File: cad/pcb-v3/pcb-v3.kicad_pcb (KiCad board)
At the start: 4 copper layers, 19.3 x 19.3 mm, 50 parts

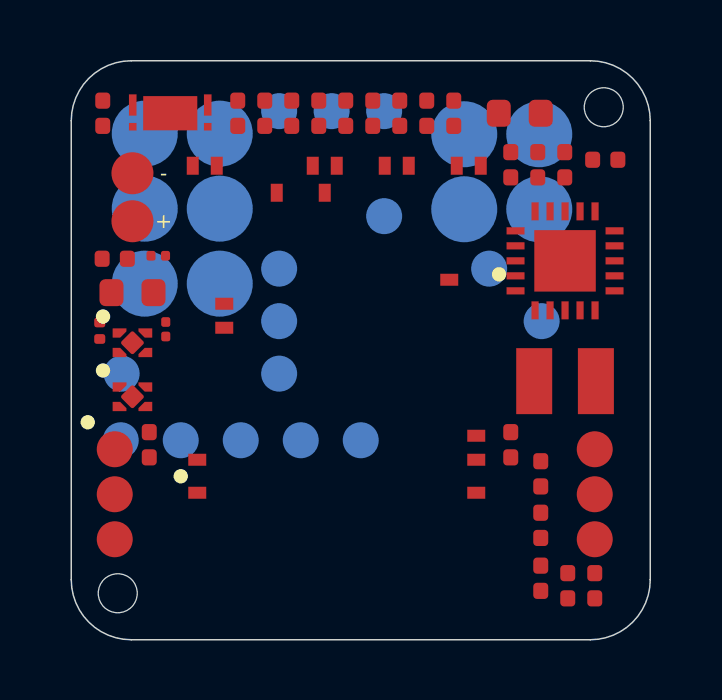
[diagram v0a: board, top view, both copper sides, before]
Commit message: Routing: 3 opens left, and none of them are the PCM's
Placing the 0201s nearest-to-U5 was the wrong objective and it was mine. It
walked R8/R9/C14 up the LEFT STRIP -- 2.72 mm wide, already carrying U3, U4
(X2SON-4, pads 0.34-0.40 apart) and C5 -- and the opens came back clustered on
exactly those parts. They are now scored by ELBOW ROOM within a bounded radius
of U5 instead.

  before: 10-12 open pads pre-stitch, 4 NO PATH after
  after :  4 open pads pre-stitch, 3 NO PATH after

PCM_VDD R8.2 and BL_RETURN R6.1 are gone -- the parts the PCM added now route.

Bounded, not free: pure elbow room threw R9 21.5 mm into the far corner, and
R9 is the V- sense leg, a high-impedance node feeding a comparator that trips
on 20 mV. Distance there is an aerial, not a resistance. SMALL_NEAR caps the
trade. Removing the cluster gate on U5 also mattered: it had dragged U5 itself
from 2.28 to 8.81 mm off the cell pad chasing a target the new objective does
not optimise.

Remaining 3 (VBAT U2.18, VBAT_OK U2.13, VSTOR U4.4) are the U2/U4 knot
ROUTING-RESULT.md named as this board's hard corner before the PCM existed --
0.5 mm-pitch QFN, 0.26 mm pad gaps, ~0.21 mm of escape ring per side. They
resist the router in six configurations and handroute at correct rules.

Also: router and gnd_taps now use 0.45/0.20 vias, JLC's documented standard
floor (preflight check 8) rather than the conservative 0.6/0.3. Taps went
16 -> 21 on the earlier board.
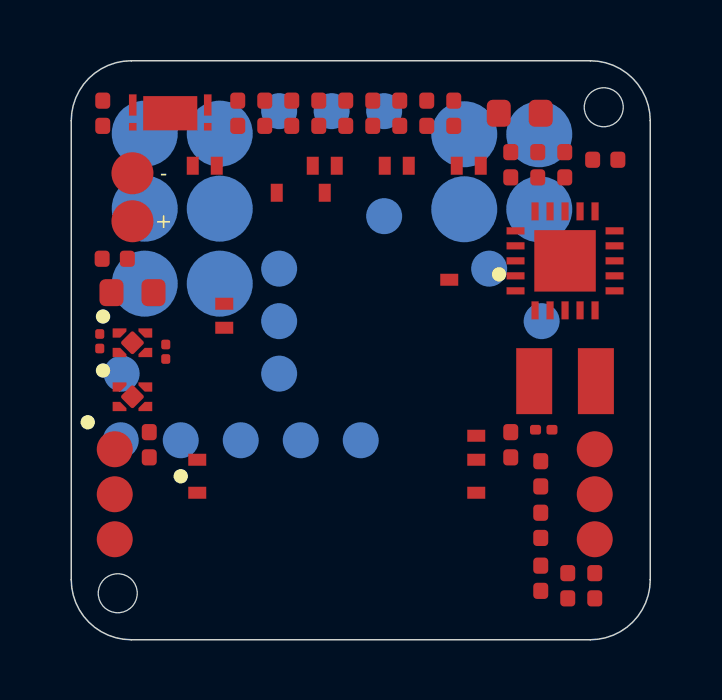
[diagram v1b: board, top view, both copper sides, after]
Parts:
- moved C14 15.2 mm to (6.10, 2.65), turned to 0 degrees
- moved R8 3.21 mm to (-6.50, 0.05), turned to 90 degrees
- moved R9 2.24 mm to (-8.70, -0.30)
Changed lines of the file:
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@@
 	(footprint "touchid:R8"
 		(layer "F.Cu")
-		(at -6.75 -3.15)
+		(at -6.5 0.05 90)
 		(property "Reference" "R8"
 			(at 0 0 0)
@@
 	(footprint "touchid:R9"
 		(layer "F.Cu")
-		(at -6.5 -0.7 90)
+		(at -8.7 -0.3 90)
 		(property "Reference" "R9"
 			(at 0 0 0)
@@
 	(footprint "touchid:C14"
 		(layer "F.Cu")
-		(at -8.7 -0.65 90)
+		(at 6.1 2.65)
 		(property "Reference" "C14"
 			(at 0 0 0)

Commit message: Fine-pitch escape ring: U3/U4 get a reserved 0.55 mm ring; 3 blockers
Five of the ten open pads were on U3/U4, and the cause was structural: they are
TPS7A2033 in X2SON-4 with pads 0.34-0.40 mm apart, so nothing routes BETWEEN
their pins at 0.127/0.10 -- every pin must escape radially. R8 sat 1.11 mm to
one side, R9 1.09 mm to the other, TP6 directly above, C5 below. U4 was boxed
in on four sides.

The packer could not know. Worse, the elbow-room objective I added earlier
actively PREFERRED those spots, because the gap beside a fine-pitch part is the
emptiest-looking space on the board. FINE_PITCH/FINE_ESCAPE now reserves a
0.55 mm ring in _legal_mask, at the source, and the 0201 objective goes back to
nearest-U5 since it no longer has to carry a job that was never its own.

  open pads 10 -> 9, and stage 1 routes 9/9 with the pogo keep-outs in place

TWO SELF-INFLICTED BUGS FOUND AND FIXED ALONG THE WAY:

* The 0201 scoring ranked by distance WITHIN a rotation and by free space
  BETWEEN rotations. Two comparisons deciding the same thing, disagreeing --
  so the fix appeared to do nothing at all and R8 stayed 21.5 mm from U5.

* check_board.py flagged copper sitting EXACTLY on the 0.10 rule: shapely
  returns 0.09999999998 and  calls that a violation, printed as
  '0.1000'. The router's own check_drc passes the same board clean. Now
  compares against MIN_CU - 1e-6; a nanometre is below any fab resolution and
  well above float noise.

Also recorded a dead end: a hand-written dangling-segment remover deleted 334
of 593 segments because its 'is this end anchored' test knew about segments and
vias but FORGOT PADS. Tracks end on pads. Reverted; the board here is the
un-stitched route, which has 9 open pads but no stubs.
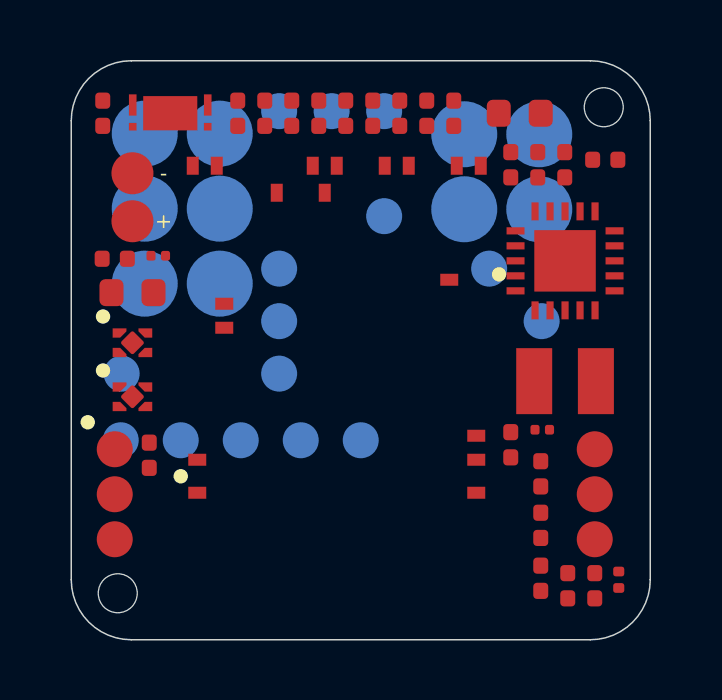
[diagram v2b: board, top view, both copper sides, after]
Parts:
- moved R9 15.0 mm to (6.05, 2.65), turned to 0 degrees
- moved C14 5.59 mm to (8.60, 7.65), turned to 90 degrees
- moved R8 3.21 mm to (-6.75, -3.15), turned to 0 degrees
- moved C8 0.35 mm to (-7.05, 3.50)
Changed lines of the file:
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@@
 	(footprint "touchid:R8"
 		(layer "F.Cu")
-		(at -6.5 0.05 90)
+		(at -6.75 -3.15)
 		(property "Reference" "R8"
 			(at 0 0 0)
@@
 	(footprint "touchid:R9"
 		(layer "F.Cu")
-		(at -8.7 -0.3 90)
+		(at 6.05 2.65)
 		(property "Reference" "R9"
 			(at 0 0 0)
@@
 	(footprint "touchid:C14"
 		(layer "F.Cu")
-		(at 6.1 2.65)
+		(at 8.6 7.65 90)
 		(property "Reference" "C14"
 			(at 0 0 0)
@@
 	(footprint "touchid:C8"
 		(layer "F.Cu")
-		(at -7.05 3.15 90)
+		(at -7.05 3.5 90)
 		(property "Reference" "C8"
 			(at 0 0 0)

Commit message: GND pads may not be ASSIGNED into a pogo no-via ring (hard ban in the packer)
The 0402/0201 assignment already had a soft _POGO_PENALTY of 40.0, reasoned
about the PART: a passive over a pogo pad has no via for its own escape and
sits where the pins flex. For a part carrying a GND pad the consequence is
harder than a penalty -- the plane is on In2.Cu, a GND pad on F.Cu reaches it
only through a via, and inside a ring no via may exist. Now a hard 1e6 cost:
104 (part, slot) pairs forbidden, and C12 moved out of J4.5's ring.

MY FIRST VERSION OF THE GLOBAL GATE WAS WRONG and I am recording why. It raised
SystemExit on any GND pad inside a ring and failed the build on EIGHT of them --
three on U1, two on U2, plus C7 and U5.4 -- all fixed-position parts that cannot
move, and most of them connected perfectly well today.

The rule I wrote was 'a GND pad may not sit in a pogo ring'. The true rule is
weaker: a GND pad needs A PATH TO GND COPPER THAT REACHES THE PLANE. Its own
via is the easy route and a ring closes it, but a track to neighbouring GND
copper does just as well -- which is exactly how U1.15, U1.32 and U2.5 are
connected right now. Being in a ring is a RISK, not a fault. Softened to a
warning that names the at-risk pads so check 6 can be read against it.

C5.2 REMAINS, and it is not a packer problem: C5 is a 0603 positioned by the
hand-written stack(), and the arithmetic says the strip cannot avoid the ring --
U3 (1.30) + U4 (1.30) + C5 (1.04) + two 0.50 gaps = 4.64 mm from y=+2.20 ends
at -2.44, while GND pads must stay above -0.795. It overruns by 1.65 mm. Three
parts do not fit above the J4 block. C5 has to leave the left strip, and where
it goes is a real design decision on a board with no spare area.
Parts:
- moved C3 15.6 mm to (6.00, 5.84)
- moved R2 12.4 mm to (3.10, -7.90)
- moved R7 8.10 mm to (-8.60, -7.90)
- moved C12 7.64 mm to (-2.30, -7.90), turned to 90 degrees
- moved R4 7.64 mm to (-8.20, -3.05), turned to 0 degrees
- moved R5 7.20 mm to (-1.40, -7.90)
- moved R6 4.50 mm to (-4.10, -7.90)
- moved ROV1 3.15 mm to (8.15, -6.35), turned to 0 degrees
- moved C6 2.70 mm to (-0.50, -7.90)
- moved C4 1.80 mm to (1.30, -7.90)
- moved C1 1.72 mm to (6.00, 4.12)
- moved ROK2 1.36 mm to (6.80, -6.18), turned to 90 degrees
- moved C10 0.93 mm to (6.90, 7.85)
- moved C2 0.93 mm to (6.00, 7.60)
- moved ROV2 0.90 mm to (5.00, -6.18)
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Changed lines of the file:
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@@
 	(footprint "touchid:C1"
 		(layer "F.Cu")
+		(at 6.0 4.119 90)
+		(property "Reference" "C1"
+			(at 0 0 0)
+			(layer "F.SilkS")
+			(hide yes)
+			(effects (font (size 0.6 0.6) (thickness 0.1)))
+		)
+		(attr smd)
+		(fp_text user "C1"
+			(at 0 0 0)
+			(layer "F.Fab")
+			(effects (font (size 0.4 0.4) (thickness 0.06)))
+		)
+		(pad "1" smd roundrect
+			(at -0.42 0)
+			(size 0.5 0.54)
+			(layers "F.Cu" "F.Mask" "F.Paste")
+			(roundrect_rratio 0.25)
+			(net 27 "VIN_DC")
+		)
+		(pad "2" smd roundrect
+			(at 0.42 0)
+			(size 0.5 0.54)
+			(layers "F.Cu" "F.Mask" "F.Paste")
+			(roundrect_rratio 0.25)
+			(net 4 "GND")
+		)
+		(model "${KIPRJMOD}/3dmodels/chip_0402.step"
+			(offset (xyz 0 0 0))
+			(scale (xyz 1 1 1))
+			(rotate (xyz 0 0 0))
+		)
+	)
+	(footprint "touchid:C2"
+		(layer "F.Cu")
+		(at 6.0 7.6 90)
+		(property "Reference" "C2"
+			(at 0 0 0)
+			(layer "F.SilkS")
+			(hide yes)
+			(effects (font (size 0.6 0.6) (thickness 0.1)))
+		)
+		(attr smd)
+		(fp_text user "C2"
+			(at 0 0 0)
+			(layer "F.Fab")
+			(effects (font (size 0.4 0.4) (thickness 0.06)))
+		)
+		(pad "1" smd roundrect
+			(at -0.42 0)
+			(size 0.5 0.54)
+			(layers "F.Cu" "F.Mask" "F.Paste")
+			(roundrect_rratio 0.25)
+			(net 30 "VSTOR")
+		)
+		(pad "2" smd roundrect
+			(at 0.42 0)
+			(size 0.5 0.54)
+			(layers "F.Cu" "F.Mask" "F.Paste")
+			(roundrect_rratio 0.25)
+			(net 4 "GND")
+		)
+		(model "${KIPRJMOD}/3dmodels/chip_0402.step"
+			(offset (xyz 0 0 0))
+			(scale (xyz 1 1 1))
+			(rotate (xyz 0 0 0))
+		)
+	)
+	(footprint "touchid:C3"
+		(layer "F.Cu")
 		(at 6.0 5.836 90)
-		(property "Reference" "C1"
-			(at 0 0 0)
-			(layer "F.SilkS")
-			(hide yes)
-			(effects (font (size 0.6 0.6) (thickness 0.1)))
-		)
-		(attr smd)
-		(fp_text user "C1"
-			(at 0 0 0)
-			(layer "F.Fab")
-			(effects (font (size 0.4 0.4) (thickness 0.06)))
-		)
-		(pad "1" smd roundrect
-			(at -0.42 0)
-			(size 0.5 0.54)
-			(layers "F.Cu" "F.Mask" "F.Paste")
-			(roundrect_rratio 0.25)
-			(net 27 "VIN_DC")
-		)
-		(pad "2" smd roundrect
-			(at 0.42 0)
-			(size 0.5 0.54)
-			(layers "F.Cu" "F.Mask" "F.Paste")
-			(roundrect_rratio 0.25)
-			(net 4 "GND")
-		)
-		(model "${KIPRJMOD}/3dmodels/chip_0402.step"
-			(offset (xyz 0 0 0))
-			(scale (xyz 1 1 1))
-			(rotate (xyz 0 0 0))
-		)
-	)
-	(footprint "touchid:C2"
-		(layer "F.Cu")
-		(at 6.9 7.85 90)
-		(property "Reference" "C2"
-			(at 0 0 0)
-			(layer "F.SilkS")
-			(hide yes)
-			(effects (font (size 0.6 0.6) (thickness 0.1)))
-		)
-		(attr smd)
-		(fp_text user "C2"
+		(property "Reference" "C3"
+			(at 0 0 0)
+			(layer "F.SilkS")
+			(hide yes)
+			(effects (font (size 0.6 0.6) (thickness 0.1)))
+		)
+		(attr smd)
+		(fp_text user "C3"
 			(at 0 0 0)
 			(layer "F.Fab")
@@
 		)
 	)
-	(footprint "touchid:C3"
-		(layer "F.Cu")
-		(at -1.4 -7.9 90)
-		(property "Reference" "C3"
-			(at 0 0 0)
-			(layer "F.SilkS")
-			(hide yes)
-			(effects (font (size 0.6 0.6) (thickness 0.1)))
-		)
-		(attr smd)
-		(fp_text user "C3"
-			(at 0 0 0)
-			(layer "F.Fab")
-			(effects (font (size 0.4 0.4) (thickness 0.06)))
-		)
-		(pad "1" smd roundrect
-			(at -0.42 0)
-			(size 0.5 0.54)
-			(layers "F.Cu" "F.Mask" "F.Paste")
-			(roundrect_rratio 0.25)
-			(net 30 "VSTOR")
-		)
-		(pad "2" smd roundrect
-			(at 0.42 0)
-			(size 0.5 0.54)
-			(layers "F.Cu" "F.Mask" "F.Paste")
-			(roundrect_rratio 0.25)
-			(net 4 "GND")
-		)
-		(model "${KIPRJMOD}/3dmodels/chip_0402.step"
-			(offset (xyz 0 0 0))
-			(scale (xyz 1 1 1))
-			(rotate (xyz 0 0 0))
-		)
-	)
 	(footprint "touchid:C4"
 		(layer "F.Cu")
-		(at 3.1 -7.9 90)
+		(at 1.3 -7.9 90)
 		(property "Reference" "C4"
 			(at 0 0 0)
@@
 	(footprint "touchid:C6"
 		(layer "F.Cu")
-		(at -3.2 -7.9 90)
+		(at -0.5 -7.9 90)
 		(property "Reference" "C6"
 			(at 0 0 0)
@@
 	(footprint "touchid:C9"
 		(layer "F.Cu")
-		(at 1.3 -7.9 90)
+		(at 0.4 -7.9 90)
 		(property "Reference" "C9"
 			(at 0 0 0)
@@
 	(footprint "touchid:C10"
 		(layer "F.Cu")
-		(at 6.0 7.6 90)
+		(at 6.9 7.85 90)
 		(property "Reference" "C10"
 			(at 0 0 0)
@@
 	(footprint "touchid:C12"
 		(layer "F.Cu")
-		(at -8.2 -3.05)
+		(at -2.3 -7.9 90)
 		(property "Reference" "C12"
 			(at 0 0 0)
@@
 	(footprint "touchid:C13"
 		(layer "F.Cu")
-		(at -4.1 -7.9 90)
+		(at -3.2 -7.9 90)
 		(property "Reference" "C13"
 			(at 0 0 0)
@@
 	(footprint "touchid:R2"
 		(layer "F.Cu")
-		(at 6.0 4.119 90)
+		(at 3.1 -7.9 90)
 		(property "Reference" "R2"
 			(at 0 0 0)
@@
 	(footprint "touchid:R4"
 		(layer "F.Cu")
-		(at -2.3 -7.9 90)
+		(at -8.2 -3.05)
 		(property "Reference" "R4"
 			(at 0 0 0)
@@
 	(footprint "touchid:R5"
 		(layer "F.Cu")
+		(at -1.4 -7.9 90)
+		(property "Reference" "R5"
+			(at 0 0 0)
+			(layer "F.SilkS")
+			(hide yes)
+			(effects (font (size 0.6 0.6) (thickness 0.1)))
+		)
+		(attr smd)
+		(fp_text user "R5"
+			(at 0 0 0)
+			(layer "F.Fab")
+			(effects (font (size 0.4 0.4) (thickness 0.06)))
+		)
+		(pad "1" smd roundrect
+			(at -0.42 0)
+			(size 0.5 0.54)
+			(layers "F.Cu" "F.Mask" "F.Paste")
+			(roundrect_rratio 0.25)
+			(net 26 "VBAT_SENSE")
+		)
+		(pad "2" smd roundrect
+			(at 0.42 0)
+			(size 0.5 0.54)
+			(layers "F.Cu" "F.Mask" "F.Paste")
+			(roundrect_rratio 0.25)
+			(net 4 "GND")
+		)
+		(model "${KIPRJMOD}/3dmodels/chip_0402.step"
+			(offset (xyz 0 0 0))
+			(scale (xyz 1 1 1))
+			(rotate (xyz 0 0 0))
+		)
+	)
+	(footprint "touchid:R6"
+		(layer "F.Cu")
+		(at -4.1 -7.9 90)
+		(property "Reference" "R6"
+			(at 0 0 0)
+			(layer "F.SilkS")
+			(hide yes)
+			(effects (font (size 0.6 0.6) (thickness 0.1)))
+		)
+		(attr smd)
+		(fp_text user "R6"
+			(at 0 0 0)
+			(layer "F.Fab")
+			(effects (font (size 0.4 0.4) (thickness 0.06)))
+		)
+		(pad "1" smd roundrect
+			(at -0.42 0)
+			(size 0.5 0.54)
+			(layers "F.Cu" "F.Mask" "F.Paste")
+			(roundrect_rratio 0.25)
+			(net 2 "BL_RETURN")
+		)
+		(pad "2" smd roundrect
+			(at 0.42 0)
+			(size 0.5 0.54)
+			(layers "F.Cu" "F.Mask" "F.Paste")
+			(roundrect_rratio 0.25)
+			(net 1 "BL_FLAG")
+		)
+		(model "${KIPRJMOD}/3dmodels/chip_0402.step"
+			(offset (xyz 0 0 0))
+			(scale (xyz 1 1 1))
+			(rotate (xyz 0 0 0))
+		)
+	)
+	(footprint "touchid:R7"
+		(layer "F.Cu")
 		(at -8.6 -7.9 90)
-		(property "Reference" "R5"
-			(at 0 0 0)
-			(layer "F.SilkS")
-			(hide yes)
-			(effects (font (size 0.6 0.6) (thickness 0.1)))
-		)
-		(attr smd)
-		(fp_text user "R5"
-			(at 0 0 0)
-			(layer "F.Fab")
-			(effects (font (size 0.4 0.4) (thickness 0.06)))
-		)
-		(pad "1" smd roundrect
-			(at -0.42 0)
-			(size 0.5 0.54)
-			(layers "F.Cu" "F.Mask" "F.Paste")
-			(roundrect_rratio 0.25)
-			(net 26 "VBAT_SENSE")
-		)
-		(pad "2" smd roundrect
-			(at 0.42 0)
-			(size 0.5 0.54)
-			(layers "F.Cu" "F.Mask" "F.Paste")
-			(roundrect_rratio 0.25)
-			(net 4 "GND")
-		)
-		(model "${KIPRJMOD}/3dmodels/chip_0402.step"
-			(offset (xyz 0 0 0))
-			(scale (xyz 1 1 1))
-			(rotate (xyz 0 0 0))
-		)
-	)
-	(footprint "touchid:R6"
-		(layer "F.Cu")
-		(at 0.4 -7.9 90)
-		(property "Reference" "R6"
-			(at 0 0 0)
-			(layer "F.SilkS")
-			(hide yes)
-			(effects (font (size 0.6 0.6) (thickness 0.1)))
-		)
-		(attr smd)
-		(fp_text user "R6"
-			(at 0 0 0)
-			(layer "F.Fab")
-			(effects (font (size 0.4 0.4) (thickness 0.06)))
-		)
-		(pad "1" smd roundrect
-			(at -0.42 0)
-			(size 0.5 0.54)
-			(layers "F.Cu" "F.Mask" "F.Paste")
-			(roundrect_rratio 0.25)
-			(net 2 "BL_RETURN")
-		)
-		(pad "2" smd roundrect
-			(at 0.42 0)
-			(size 0.5 0.54)
-			(layers "F.Cu" "F.Mask" "F.Paste")
-			(roundrect_rratio 0.25)
-			(net 1 "BL_FLAG")
-		)
-		(model "${KIPRJMOD}/3dmodels/chip_0402.step"
-			(offset (xyz 0 0 0))
-			(scale (xyz 1 1 1))
-			(rotate (xyz 0 0 0))
-		)
-	)
-	(footprint "touchid:R7"
-		(layer "F.Cu")
-		(at -0.5 -7.9 90)
 		(property "Reference" "R7"
 			(at 0 0 0)
@@
 	(footprint "touchid:ROV1"
 		(layer "F.Cu")
+		(at 8.15 -6.35)
+		(property "Reference" "ROV1"
+			(at 0 0 0)
+			(layer "F.SilkS")
+			(hide yes)
+			(effects (font (size 0.6 0.6) (thickness 0.1)))
+		)
+		(attr smd)
+		(fp_text user "ROV1"
+			(at 0 0 0)
+			(layer "F.Fab")
+			(effects (font (size 0.4 0.4) (thickness 0.06)))
+		)
+		(pad "1" smd roundrect
+			(at -0.42 0)
+			(size 0.5 0.54)
+			(layers "F.Cu" "F.Mask" "F.Paste")
+			(roundrect_rratio 0.25)
+			(net 25 "VBAT_OV_SET")
+		)
+		(pad "2" smd roundrect
+			(at 0.42 0)
+			(size 0.5 0.54)
+			(layers "F.Cu" "F.Mask" "F.Paste")
+			(roundrect_rratio 0.25)
+			(net 4 "GND")
+		)
+		(model "${KIPRJMOD}/3dmodels/chip_0402.step"
+			(offset (xyz 0 0 0))
+			(scale (xyz 1 1 1))
+			(rotate (xyz 0 0 0))
+		)
+	)
+	(footprint "touchid:ROV2"
+		(layer "F.Cu")
 		(at 5.0 -6.183 90)
-		(property "Reference" "ROV1"
-			(at 0 0 0)
-			(layer "F.SilkS")
-			(hide yes)
-			(effects (font (size 0.6 0.6) (thickness 0.1)))
-		)
-		(attr smd)
-		(fp_text user "ROV1"
-			(at 0 0 0)
-			(layer "F.Fab")
-			(effects (font (size 0.4 0.4) (thickness 0.06)))
-		)
-		(pad "1" smd roundrect
-			(at -0.42 0)
-			(size 0.5 0.54)
-			(layers "F.Cu" "F.Mask" "F.Paste")
-			(roundrect_rratio 0.25)
-			(net 25 "VBAT_OV_SET")
-		)
-		(pad "2" smd roundrect
-			(at 0.42 0)
-			(size 0.5 0.54)
-			(layers "F.Cu" "F.Mask" "F.Paste")
-			(roundrect_rratio 0.25)
-			(net 4 "GND")
-		)
-		(model "${KIPRJMOD}/3dmodels/chip_0402.step"
-			(offset (xyz 0 0 0))
-			(scale (xyz 1 1 1))
-			(rotate (xyz 0 0 0))
-		)
-	)
-	(footprint "touchid:ROV2"
-		(layer "F.Cu")
-		(at 5.9 -6.183 90)
 		(property "Reference" "ROV2"
 			(at 0 0 0)
@@
 	(footprint "touchid:ROK2"
 		(layer "F.Cu")
-		(at 8.15 -6.35)
+		(at 6.8 -6.183 90)
 		(property "Reference" "ROK2"
 			(at 0 0 0)
@@
 	(footprint "touchid:ROK3"
 		(layer "F.Cu")
-		(at 6.8 -6.183 90)
+		(at 5.9 -6.183 90)
 		(property "Reference" "ROK3"
 			(at 0 0 0)
